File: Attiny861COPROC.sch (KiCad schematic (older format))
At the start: 3 parts

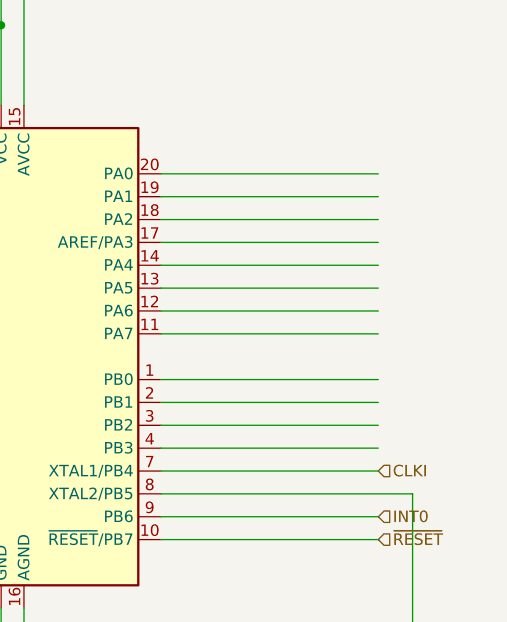
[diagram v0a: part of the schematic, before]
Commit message: Breakout other lines
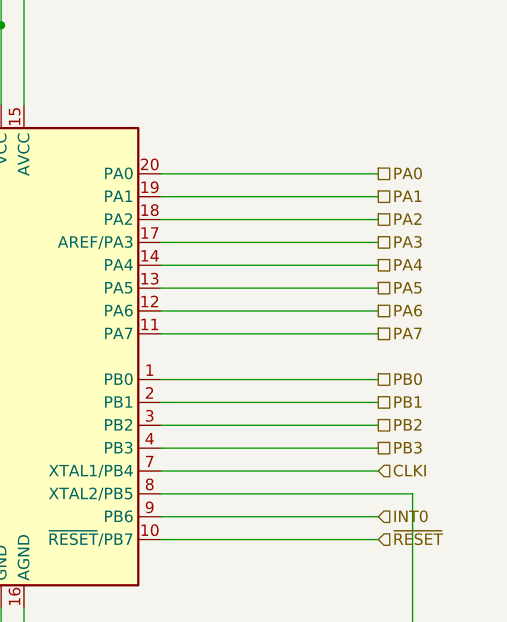
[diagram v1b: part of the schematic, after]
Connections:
- net labels added: PA0, PA1, PA2, PA3, PA4, PA5, PA6, PA7, PB0, PB1, PB2, PB3
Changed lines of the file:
@@
 Text HLabel 5350 3700 2    50   Input ~ 0
 ~RESET
+Text HLabel 5350 2100 2    50   UnSpc ~ 0
+PA0
+Text HLabel 5350 2200 2    50   UnSpc ~ 0
+PA1
+Text HLabel 5350 2300 2    50   UnSpc ~ 0
+PA2
+Text HLabel 5350 2400 2    50   UnSpc ~ 0
+PA3
+Text HLabel 5350 2500 2    50   UnSpc ~ 0
+PA4
+Text HLabel 5350 2600 2    50   UnSpc ~ 0
+PA5
+Text HLabel 5350 2700 2    50   UnSpc ~ 0
+PA6
+Text HLabel 5350 2800 2    50   UnSpc ~ 0
+PA7
+Text HLabel 5350 3000 2    50   UnSpc ~ 0
+PB0
+Text HLabel 5350 3100 2    50   UnSpc ~ 0
+PB1
+Text HLabel 5350 3200 2    50   UnSpc ~ 0
+PB2
+Text HLabel 5350 3300 2    50   UnSpc ~ 0
+PB3
 $EndSCHEMATC

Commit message: fixup int0 for the attiny861 to be pb6
Add a second attiny861
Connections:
- net INT0 renamed PB6
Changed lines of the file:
@@
 AR Path="/7B8F07E9" Ref="U?"  Part="1"
 AR Path="/7B77DBC0/7B8F07E9" Ref="U?"  Part="1"
+AR Path="/7C66C7D3/7B8F07E9" Ref="U?"  Part="1"
 F 0 "U?" H 3071 2946 50  0000 R CNN
 F 1 "ATtiny861-20PU" H 3071 2855 50  0000 R CNN
@@
 AR Path="/7B8F07F4" Ref="C?"  Part="1"
 AR Path="/7B77DBC0/7B8F07F4" Ref="C?"  Part="1"
+AR Path="/7C66C7D3/7B8F07F4" Ref="C?"  Part="1"
 F 0 "C?" H 2965 3796 50  0000 L CNN
 F 1 "0.1uF" H 2965 3705 50  0000 L CNN
@@
 AR Path="/7B8F07FB" Ref="C?"  Part="1"
 AR Path="/7B77DBC0/7B8F07FB" Ref="C?"  Part="1"
+AR Path="/7C66C7D3/7B8F07FB" Ref="C?"  Part="1"
 F 0 "C?" H 2515 3796 50  0000 L CNN
 F 1 "0.1uF" H 2515 3705 50  0000 L CNN
@@
 AR Path="/7B8F0809" Ref="#PWR?"  Part="1"
 AR Path="/7B77DBC0/7B8F0809" Ref="#PWR?"  Part="1"
+AR Path="/7C66C7D3/7B8F0809" Ref="#PWR?"  Part="1"
 F 0 "#PWR?" H 3700 4450 50  0001 C CNN
 F 1 "GND" H 3705 4527 50  0000 C CNN
@@
 AR Path="/7B8F080F" Ref="#PWR?"  Part="1"
 AR Path="/7B77DBC0/7B8F080F" Ref="#PWR?"  Part="1"
+AR Path="/7C66C7D3/7B8F080F" Ref="#PWR?"  Part="1"
 F 0 "#PWR?" H 3800 4150 50  0001 C CNN
 F 1 "GND" H 3805 4227 50  0000 C CNN
@@
 AR Path="/7B8F081B" Ref="#PWR?"  Part="1"
 AR Path="/7B77DBC0/7B8F081B" Ref="#PWR?"  Part="1"
+AR Path="/7C66C7D3/7B8F081B" Ref="#PWR?"  Part="1"
 F 0 "#PWR?" H 3700 950 50  0001 C CNN
 F 1 "+5V" H 3715 1273 50  0000 C CNN
@@
 AR Path="/7B8F0821" Ref="#PWR?"  Part="1"
 AR Path="/7B77DBC0/7B8F0821" Ref="#PWR?"  Part="1"
+AR Path="/7C66C7D3/7B8F0821" Ref="#PWR?"  Part="1"
 F 0 "#PWR?" H 4000 950 50  0001 C CNN
 F 1 "+5V" H 4015 1273 50  0000 C CNN
@@
 AR Path="/7B8F083A" Ref="#PWR?"  Part="1"
 AR Path="/7B77DBC0/7B8F083A" Ref="#PWR?"  Part="1"
+AR Path="/7C66C7D3/7B8F083A" Ref="#PWR?"  Part="1"
 F 0 "#PWR?" H 5500 4000 50  0001 C CNN
 F 1 "GND" H 5505 4077 50  0000 C CNN
@@
 Text HLabel 5350 3400 2    50   Input ~ 0
 CLKI
-Text HLabel 5350 3600 2    50   Input ~ 0
-INT0
+Text HLabel 5350 3600 2    50   UnSpc ~ 0
+PB6
 Text HLabel 5350 3700 2    50   Input ~ 0
 ~RESET

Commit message: We always have access to the 861s
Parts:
- gave numbers to parts that had none: 3
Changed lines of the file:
@@
 $Descr A4 11693 8268
 encoding utf-8
-Sheet 2 2
+Sheet 2 3
 Title "ATTINY861 Synchronized Coprocessor"
 Date "2021-10-16"
@@
 P 3700 2900
 AR Path="/7B8F07E9" Ref="U?"  Part="1"
-AR Path="/7B77DBC0/7B8F07E9" Ref="U?"  Part="1"
-AR Path="/7C66C7D3/7B8F07E9" Ref="U?"  Part="1"
-F 0 "U?" H 3071 2946 50  0000 R CNN
+AR Path="/7B77DBC0/7B8F07E9" Ref="U18"  Part="1"
+AR Path="/7C66C7D3/7B8F07E9" Ref="U19"  Part="1"
+F 0 "U18" H 3071 2946 50  0000 R CNN
 F 1 "ATtiny861-20PU" H 3071 2855 50  0000 R CNN
 F 2 "Package_DIP:DIP-20_W7.62mm_Socket" H 3700 2900 50  0001 C CIN
@@
 	3700 1800 3700 1450
 Wire Wire Line
-	3700 1450 2850 1450
+	3700 1450 3550 1450
 Wire Wire Line
 	2850 1450 2850 3600
@@
 P 2850 3750
 AR Path="/7B8F07F4" Ref="C?"  Part="1"
-AR Path="/7B77DBC0/7B8F07F4" Ref="C?"  Part="1"
-AR Path="/7C66C7D3/7B8F07F4" Ref="C?"  Part="1"
-F 0 "C?" H 2965 3796 50  0000 L CNN
+AR Path="/7B77DBC0/7B8F07F4" Ref="C28"  Part="1"
+AR Path="/7C66C7D3/7B8F07F4" Ref="C30"  Part="1"
+F 0 "C28" H 2965 3796 50  0000 L CNN
 F 1 "0.1uF" H 2965 3705 50  0000 L CNN
 F 2 "Capacitor_SMD:C_0805_2012Metric_Pad1.18x1.45mm_HandSolder" H 2888 3600 50  0001 C CNN
@@
 P 2400 3750
 AR Path="/7B8F07FB" Ref="C?"  Part="1"
-AR Path="/7B77DBC0/7B8F07FB" Ref="C?"  Part="1"
-AR Path="/7C66C7D3/7B8F07FB" Ref="C?"  Part="1"
-F 0 "C?" H 2515 3796 50  0000 L CNN
+AR Path="/7B77DBC0/7B8F07FB" Ref="C27"  Part="1"
+AR Path="/7C66C7D3/7B8F07FB" Ref="C29"  Part="1"
+F 0 "C27" H 2515 3796 50  0000 L CNN
 F 1 "0.1uF" H 2515 3705 50  0000 L CNN
 F 2 "Capacitor_SMD:C_0805_2012Metric_Pad1.18x1.45mm_HandSolder" H 2438 3600 50  0001 C CNN
@@
 P 3700 4700
 AR Path="/7B8F0809" Ref="#PWR?"  Part="1"
-AR Path="/7B77DBC0/7B8F0809" Ref="#PWR?"  Part="1"
-AR Path="/7C66C7D3/7B8F0809" Ref="#PWR?"  Part="1"
-F 0 "#PWR?" H 3700 4450 50  0001 C CNN
+AR Path="/7B77DBC0/7B8F0809" Ref="#PWR066"  Part="1"
+AR Path="/7C66C7D3/7B8F0809" Ref="#PWR073"  Part="1"
+F 0 "#PWR066" H 3700 4450 50  0001 C CNN
 F 1 "GND" H 3705 4527 50  0000 C CNN
 F 2 "" H 3700 4700 50  0001 C CNN
@@
 P 3800 4400
 AR Path="/7B8F080F" Ref="#PWR?"  Part="1"
-AR Path="/7B77DBC0/7B8F080F" Ref="#PWR?"  Part="1"
-AR Path="/7C66C7D3/7B8F080F" Ref="#PWR?"  Part="1"
-F 0 "#PWR?" H 3800 4150 50  0001 C CNN
+AR Path="/7B77DBC0/7B8F080F" Ref="#PWR068"  Part="1"
+AR Path="/7C66C7D3/7B8F080F" Ref="#PWR075"  Part="1"
+F 0 "#PWR068" H 3800 4150 50  0001 C CNN
 F 1 "GND" H 3805 4227 50  0000 C CNN
 F 2 "" H 3800 4400 50  0001 C CNN
@@
 Connection ~ 3800 4400
 Wire Wire Line
-	3700 1450 3700 1100
-Connection ~ 3700 1450
-Wire Wire Line
-	3800 1300 4000 1300
-Wire Wire Line
-	4000 1300 4000 1100
-Connection ~ 3800 1300
-$Comp
-L power:+5V #PWR?
-U 1 1 7B8F081B
-P 3700 1100
-AR Path="/640CD6D6/7B8F081B" Ref="#PWR?"  Part="1"
-AR Path="/7B8F081B" Ref="#PWR?"  Part="1"
-AR Path="/7B77DBC0/7B8F081B" Ref="#PWR?"  Part="1"
-AR Path="/7C66C7D3/7B8F081B" Ref="#PWR?"  Part="1"
-F 0 "#PWR?" H 3700 950 50  0001 C CNN
-F 1 "+5V" H 3715 1273 50  0000 C CNN
-F 2 "" H 3700 1100 50  0001 C CNN
-F 3 "" H 3700 1100 50  0001 C CNN
-	1    3700 1100
-	1    0    0    -1
-$EndComp
-$Comp
-L power:+5V #PWR?
-U 1 1 7B8F0821
-P 4000 1100
-AR Path="/640CD6D6/7B8F0821" Ref="#PWR?"  Part="1"
-AR Path="/7B8F0821" Ref="#PWR?"  Part="1"
-AR Path="/7B77DBC0/7B8F0821" Ref="#PWR?"  Part="1"
-AR Path="/7C66C7D3/7B8F0821" Ref="#PWR?"  Part="1"
-F 0 "#PWR?" H 4000 950 50  0001 C CNN
-F 1 "+5V" H 4015 1273 50  0000 C CNN
-F 2 "" H 4000 1100 50  0001 C CNN
-F 3 "" H 4000 1100 50  0001 C CNN
-	1    4000 1100
-	1    0    0    -1
-$EndComp
-Wire Wire Line
 	4400 2100 5350 2100
 Wire Wire Line
@@
 P 5500 4250
 AR Path="/7B8F083A" Ref="#PWR?"  Part="1"
-AR Path="/7B77DBC0/7B8F083A" Ref="#PWR?"  Part="1"
-AR Path="/7C66C7D3/7B8F083A" Ref="#PWR?"  Part="1"
-F 0 "#PWR?" H 5500 4000 50  0001 C CNN
+AR Path="/7B77DBC0/7B8F083A" Ref="#PWR071"  Part="1"
+AR Path="/7C66C7D3/7B8F083A" Ref="#PWR078"  Part="1"
+F 0 "#PWR071" H 5500 4000 50  0001 C CNN
 F 1 "GND" H 5505 4077 50  0000 C CNN
 F 2 "" H 5500 4250 50  0001 C CNN
@@
 Text HLabel 5350 3300 2    50   UnSpc ~ 0
 PB3
+Connection ~ 3800 1300
+Wire Wire Line
+	3550 1150 3550 1450
+Connection ~ 3550 1450
+Wire Wire Line
+	3550 1450 2850 1450
+Wire Wire Line
+	3800 1150 3800 1300
+$Comp
+L power:+5V #PWR?
+U 1 1 7D8C243B
+P 3800 1150
+F 0 "#PWR?" H 3800 1000 50  0001 C CNN
+F 1 "+5V" H 3815 1323 50  0000 C CNN
+F 2 "" H 3800 1150 50  0001 C CNN
+F 3 "" H 3800 1150 50  0001 C CNN
+	1    3800 1150
+	1    0    0    -1
+$EndComp
+$Comp
+L power:+5V #PWR?
+U 1 1 7D8C24C0
+P 3550 1150
+F 0 "#PWR?" H 3550 1000 50  0001 C CNN
+F 1 "+5V" H 3565 1323 50  0000 C CNN
+F 2 "" H 3550 1150 50  0001 C CNN
+F 3 "" H 3550 1150 50  0001 C CNN
+	1    3550 1150
+	1    0    0    -1
+$EndComp
 $EndSCHEMATC
